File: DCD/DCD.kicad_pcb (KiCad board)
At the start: 4 copper layers, 110 x 110 mm, 141 parts, among them J1 UMPS-04-03.5-G-VT-SM-WT, J2 UMPS-04-03.5-G-VT-SM-WT, J3 UMPS-04-03.5-G-VT-SM-WT, J4 UMPS-04-03.5-G-VT-SM-WT, U1 TLV76780DBVR, U10 OPA277UA, U11 DAC8811ICDGKT, U12 DAC8811ICDGKT, U13 OPA277UA, U14 OPA277UA, U2 ADP7182AUJZ-1.8-R7, U3 LP2985-50DBVR, U4 LP2985-18DBVR, U5 LP2985-33DBVR, U6 ADR4550BRZ, U7 ADA4945-1ACPZ-R2, U8 ADA4945-1ACPZ-R2, U9 AD4630-24BBCZ

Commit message: Progress on the layout
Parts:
- removed C20, C21, C22, C23, C26: 100p, Capacitor_SMD:C_0603_1608Metric
- removed C24: 1µF, Capacitor_SMD:C_0603_1608Metric
- removed C25, C34, C35: 1nF, Capacitor_SMD:C_0603_1608Metric
- removed FB17: 470Ω, Inductor_SMD:L_0603_1608Metric
- removed R1, R2, R3, R4, R5, R6, R7, R8, R9: 1k, Resistor_SMD:R_0603_1608Metric
- removed R12, R13: 100, Resistor_SMD:R_0603_1608Metric
- removed TP3: TestPoint, TestPoint:TestPoint_Pad_D1.5mm
- removed U7, U8: ADA4945-1ACPZ-R2, custom_components:LFCSP16_ADA4945-1ACPZ-R2_ADI
- added FB11: 470Ω, Inductor_SMD:L_0603_1608Metric, F.Cu at (159.3, 54.8)
- added FB18: 470Ω, Inductor_SMD:L_0603_1608Metric, F.Cu at (170.2, 59.8)
- added FB19: 470Ω, Inductor_SMD:L_0603_1608Metric, F.Cu at (181.5, 86.2)
- added FB20: 470Ω, Inductor_SMD:L_0603_1608Metric, F.Cu at (149.8, 103.8)
- added J5: Conn_01x02_Pin, Connector_PinHeader_2.54mm:PinHeader_1x02_P2.54mm_Vertical, F.Cu at (159.2, 51.5)
- added N4: M3 Thumbnut, custom_components:ThumbNut-M3, F.Cu at (175.7, 124.1)
- B1: footprint LOBSTER:Screw_DIN933_M3x14mm -> custom_components:Screw_DIN933_M3x14mm
- H15: footprint LOBSTER:ThreadedSpacer_6mm_M3x0.5_5mm -> custom_components:ThreadedSpacer_6mm_M3x0.5_5mm
- N1, N2, N3, N5, N6, N7: footprint LOBSTER:ThumbNut-M3 -> custom_components:ThumbNut-M3
- moved C28 162.3 mm to (178.2, 88.2), turned to 90 degrees
- moved C27 161.0 mm to (176.8, 88.2), turned to 90 degrees
- moved FB12 156.2 mm to (178.2, 111.2)
- moved C29 150.4 mm to (167.8, 87.2), turned to 90 degrees
- moved FB15 138.8 mm to (160.8, 120.8), turned to -135 degrees
- moved C32 138.8 mm to (153.2, 99.8), turned to 45 degrees
- moved U6 138.0 mm to (172.2, 88.8), turned to 180 degrees
- moved C7 135.2 mm to (165.4, 128.5), turned to 180 degrees
- moved C14 134.5 mm to (164.1, 133.5)
- moved C36 134.2 mm to (153.0, 90.5), turned to 45 degrees
- moved FB7 134.1 mm to (151.7, 101.8), turned to 135 degrees
- moved C12 132.7 mm to (160.9, 132.0), turned to 90 degrees
- moved U13 131.6 mm to (172.5, 76.2), turned to 180 degrees
- moved C10 131.5 mm to (162.4, 128.5)
- moved FB3 131.4 mm to (159.4, 135.2), turned to 180 degrees
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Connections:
- C1 pad 2: /ADC/GND -> /ADC/DGND
- C10 pad 1: /ADC/GND -> /ADC/DGND
- C11 pad 1: /ADC/GND -> /ADC/DGND
- C12 pad 2: /ADC/GND -> /ADC/DGND
- C13 pad 2: /ADC/GND -> /ADC/DGND
- C14 pad 2: /ADC/GND -> /ADC/DGND
- C15 pad 2: /ADC/GND -> /ADC/DGND
- C16 pad 2: /ADC/GND -> /ADC/DGND
- C17 pad 1: /ADC/GND -> /ADC/DGND
- C18 pad 2: /ADC/GND -> /ADC/DGND
- C19 pad 2: /ADC/GND -> /ADC/DGND
- C2 pad 2: /ADC/GND -> /ADC/DGND
- C27 pad 2: /ADC/GND -> /ADC/AGND
- C28 pad 2: /ADC/GND -> /ADC/AGND
- C29 pad 2: /ADC/GND -> /ADC/AGND
- C3 pad 2: /ADC/GND -> /ADC/DGND
- C30 pad 2: /ADC/GND -> /ADC/AGND
- C31 pad 2: /ADC/GND -> /ADC/AGND
- C32 pad 2: /ADC/GND -> /ADC/AGND
- C33 pad 2: /ADC/GND -> /ADC/AGND
- C36 pad 1: Net-(U9-IN0-) -> Net-(U9-IN0+)
- C36 pad 2: /ADC/GND -> /ADC/AGND
- C37 pad 1: Net-(U9-IN1-) -> Net-(U9-IN1+)
- C37 pad 2: /ADC/GND -> /ADC/AGND
- C38 pad 2: /ADC/GND -> /ADC/DGND
- C39 pad 2: /ADC/GND -> /ADC/DGND
- C4 pad 2: /ADC/GND -> /ADC/DGND
- C40 pad 2: /ADC/GND -> /ADC/DGND
- C41 pad 2: /ADC/GND -> /ADC/DGND
- C42 pad 2: /ADC/GND -> /ADC/DGND
- C43 pad 2: /ADC/GND -> /ADC/DGND
- C46 pad 2: /ADC/GND -> /ADC/AGND
- C47 pad 2: /ADC/GND -> /ADC/AGND
- C48 pad 2: /ADC/GND -> /ADC/AGND
- C49 pad 2: /ADC/GND -> /ADC/AGND
- C5 pad 2: /ADC/GND -> /ADC/DGND
- C50 pad 2: /ADC/GND -> /ADC/AGND
- C51 pad 1: /PSUs/-1.8V -> /DAC/-1.2V
- C51 pad 2: /ADC/GND -> /ADC/DGND
- C52 pad 2: /ADC/GND -> /ADC/DGND
- C53 pad 2: /ADC/GND -> /ADC/DGND
- C54 pad 2: /ADC/GND -> /ADC/DGND
- C55 pad 2: /ADC/GND -> /ADC/DGND
- C56 pad 2: /ADC/GND -> /ADC/DGND
- C6 pad 2: /ADC/GND -> /ADC/DGND
- C7 pad 2: /ADC/GND -> /ADC/DGND
- C8 pad 2: /ADC/GND -> /ADC/DGND
- C9 pad 2: /ADC/GND -> /ADC/DGND
- FB2 pad 2: /PSUs/-1.8V -> /DAC/-1.2V
- J2 pad 2: Net-(J2-Pin_2) -> /ADC/DGND
- J4 pad 2: /ADC/GND -> /ADC/AGND
- JP1 pad 3: /ADC/GND -> /ADC/AGND
- R14 pad 1: Net-(U7--OUT) -> /ADC/IN0
- R14 pad 2: Net-(U9-IN0-) -> Net-(U9-IN0+)
- R15 pad 1: Net-(U8--OUT) -> /ADC/IN1
- R15 pad 2: Net-(U9-IN1-) -> Net-(U9-IN1+)
- R17 pad 2: /ADC/GND -> /ADC/AGND
- U1 pad 2: /ADC/GND -> /ADC/DGND
- U10 pad 4: /ADC/GND -> /ADC/AGND
- U11 pad 6: /ADC/GND -> /ADC/AGND
- U12 pad 6: /ADC/GND -> /ADC/AGND
- U13 pad 3: /ADC/GND -> /ADC/AGND
- U14 pad 3: /ADC/GND -> /ADC/AGND
- U2 pad 1: /ADC/GND -> /ADC/DGND
- U3 pad 2: /ADC/GND -> /ADC/DGND
- U4 pad 2: /ADC/GND -> /ADC/DGND
- U5 pad 2: /ADC/GND -> /ADC/DGND
- U6 pad 4: /ADC/GND -> /ADC/AGND
- U9 pad A1: /ADC/GND -> /ADC/AGND
- U9 pad A4: /ADC/GND -> /ADC/AGND
- U9 pad A5: /ADC/GND -> /ADC/AGND
- U9 pad B2: /ADC/GND -> /ADC/AGND
- U9 pad B4: /ADC/GND -> /ADC/AGND
- U9 pad B5: /ADC/GND -> /ADC/AGND
- U9 pad B6: /ADC/GND -> /ADC/DGND
- U9 pad B7: /ADC/GND -> /ADC/DGND
- U9 pad C1: Net-(U9-IN0-) -> /ADC/AGND
- U9 pad C2: /ADC/GND -> /ADC/AGND
- U9 pad C3: /ADC/GND -> /ADC/AGND
- U9 pad C4: /ADC/GND -> /ADC/AGND
- U9 pad C5: /ADC/GND -> /ADC/AGND
- U9 pad C6: /ADC/GND -> /ADC/DGND
- U9 pad D1: /ADC/GND -> /ADC/AGND
- U9 pad D4: /ADC/GND -> /ADC/AGND
- U9 pad D5: /ADC/GND -> /ADC/AGND
- U9 pad D6: /ADC/GND -> /ADC/DGND
- U9 pad E1: /ADC/GND -> /ADC/AGND
- U9 pad E4: /ADC/GND -> /ADC/AGND
- U9 pad E5: /ADC/GND -> /ADC/AGND
- U9 pad E6: /ADC/GND -> /ADC/DGND
- U9 pad E7: /ADC/GND -> /ADC/DGND
- U9 pad F2: /ADC/GND -> /ADC/AGND
- U9 pad F3: /ADC/GND -> /ADC/AGND
- U9 pad F4: /ADC/GND -> /ADC/AGND
- U9 pad F5: /ADC/GND -> /ADC/AGND
- U9 pad F6: /ADC/GND -> /ADC/DGND
- U9 pad G1: Net-(U9-IN1-) -> /ADC/AGND
- U9 pad G2: /ADC/GND -> /ADC/AGND
- U9 pad G4: /ADC/GND -> /ADC/AGND
- U9 pad G5: /ADC/GND -> /ADC/AGND
- U9 pad G6: /ADC/GND -> /ADC/DGND
- U9 pad H1: /ADC/GND -> /ADC/AGND
- U9 pad H2: /ADC/GND -> /ADC/AGND
- U9 pad H4: /ADC/GND -> /ADC/AGND
- U9 pad H8: /ADC/GND -> /ADC/DGND
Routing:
- net Net-(U1-OUT): track 0.00 -> 195.6 mm
- net Net-(U3-VOUT): track 0.00 -> 70.2 mm
- net /ADC/7V: track 0.00 -> 59.7 mm
- net /ADC/5V: track 0.00 -> 47.9 mm, vias 0 -> 2
- net /ADC/1.8V: track 0.00 -> 47.2 mm
- net /Comms/DAC_Ext: track 0.00 -> 36.8 mm, vias 0 -> 1
- net /DAC/DAC1: track 0.00 -> 35.2 mm
- net /ADC/SDO0: track 0.00 -> 27.6 mm, vias 0 -> 1
- net /ADC/BSY: track 0.00 -> 26.8 mm, vias 0 -> 1
- net /ADC/~{CS}: track 0.00 -> 25.6 mm, vias 0 -> 1
- net Net-(U6-VOUT): track 0.00 -> 24.2 mm
- net /ADC/SDI: track 0.00 -> 18.4 mm
- net /DAC/3.3V: track 0.00 -> 14.8 mm
- net /ADC/SCK: track 0.00 -> 14.4 mm
- net Net-(J3-Pin_4): track 0.00 -> 13.8 mm, vias 0 -> 1
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
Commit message: Pregrezz
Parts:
- removed the FB11 at (124.0, 102.5)
- moved FB15 6.10 mm to (164.2, 115.8)
- moved C49 2.76 mm to (156.8, 62.0)
- moved FB18 2.24 mm to (171.2, 61.8)
- moved FB20 1.41 mm to (148.8, 102.8)
- moved FB19 0.79 mm to (181.8, 87.0)
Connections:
- J3 pad 1: Net-(J3-Pin_1) -> /Comms/CLK
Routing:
- net /DAC/-1.2V: track 6.26 -> 89.2 mm, vias 0 -> 2
- net /DAC/3.3V: track 14.8 -> 82.1 mm
- net /Comms/VRef: track 0.02 -> 60.6 mm, vias 1 -> 3
- net /ADC/VIO: track 6.01 -> 61.5 mm, vias 0 -> 2
- net Net-(U6-VOUT): track 24.2 -> 74.0 mm, vias 0 -> 2
- net /ADC/7V: track 59.7 -> 79.5 mm, vias 0 -> 4
- net Net-(U1-OUT): track 195.6 -> 199.0 mm
- net /ADC/5V: vias 2 -> 4
- net /ADC/DGND: vias 3 -> 15
- net /ADC/AGND: vias 6 -> 37

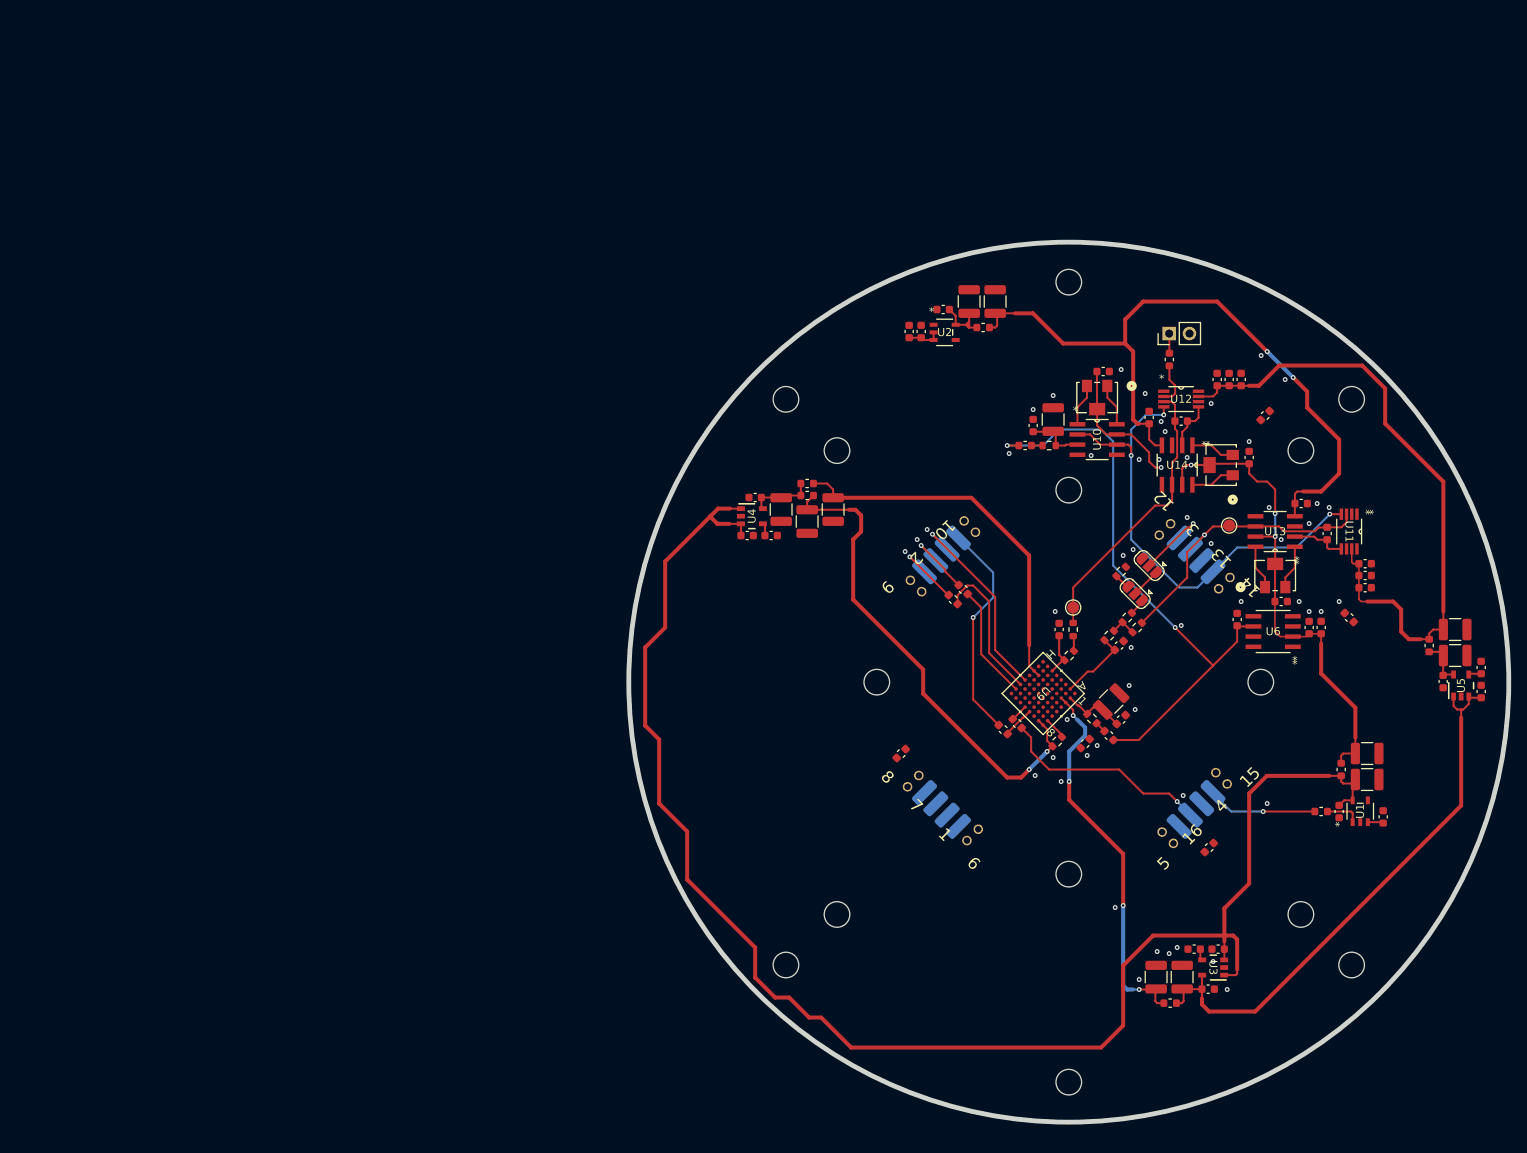
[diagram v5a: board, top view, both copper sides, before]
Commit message: Schematics for the clock reconditioning
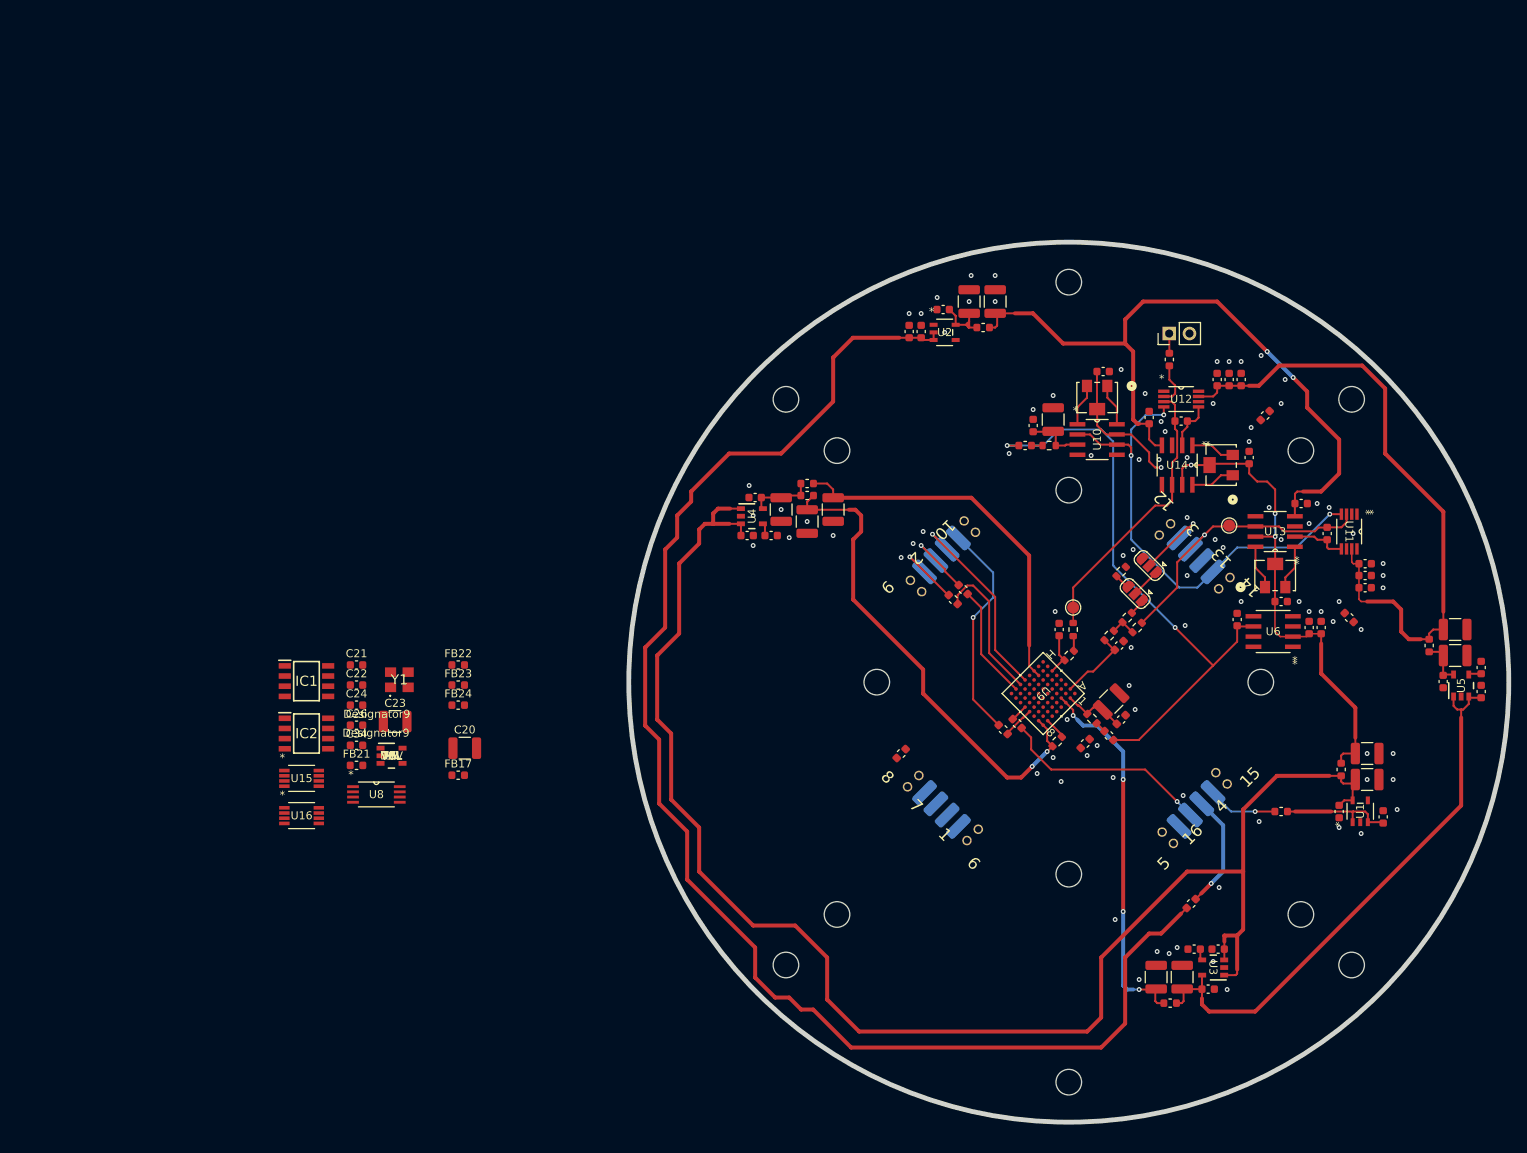
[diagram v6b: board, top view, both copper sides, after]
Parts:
- added C20: 10uF, Capacitor_SMD:C_1210_3225Metric, F.Cu at (71.2, 103.3)
- added C21: 1µF, Capacitor_SMD:C_0603_1608Metric, F.Cu at (57.7, 92.9)
- added C22: 10nF, Capacitor_SMD:C_0603_1608Metric, F.Cu at (57.7, 95.4)
- added C23: 10uF, Capacitor_SMD:C_1210_3225Metric, F.Cu at (62.5, 100.0)
- added C24: 100nF, Capacitor_SMD:C_0603_1608Metric, F.Cu at (57.7, 98.0)
- added C26: 1µF, Capacitor_SMD:C_0603_1608Metric, F.Cu at (57.7, 100.5)
- added C34: 100nF, Capacitor_SMD:C_0603_1608Metric, F.Cu at (57.7, 103.0)
- added FB17: 470Ω, Inductor_SMD:L_0603_1608Metric, F.Cu at (70.4, 106.7)
- added FB21: 470Ω, Inductor_SMD:L_0603_1608Metric, F.Cu at (57.7, 105.5)
- added FB22: 470Ω, Inductor_SMD:L_0603_1608Metric, F.Cu at (70.4, 92.9)
- added FB23: 470Ω, Inductor_SMD:L_0603_1608Metric, F.Cu at (70.4, 95.4)
- added FB24: 470Ω, Inductor_SMD:L_0603_1608Metric, F.Cu at (70.4, 98.0)
- added IC1: 830S21AMI-01LF, custom_components:SOIC127P600X175-8N, F.Cu at (51.4, 95.0)
- added IC2: 830S21AMI-01LF, custom_components:SOIC127P600X175-8N, F.Cu at (51.4, 101.5)
- added U15: MC100EP31DTG, custom_components:TSSOP8_3P10X3P10_ONS, F.Cu at (50.8, 107.1)
- added U16: MC100EP31DTG, custom_components:TSSOP8_3P10X3P10_ONS, F.Cu at (50.8, 111.8)
- added U7: LP2985-33DBVR, custom_components:DBV0005A_N, F.Cu at (62.1, 104.3)
- added U8: CDCLVC1104PWR, custom_components:PW8, F.Cu at (60.2, 109.1)
- added Y1: SiT8208AI-21-33E-50.000000, custom_components:QFN_3225_4pins, F.Cu at (63.0, 94.8)
- moved FB15 7.35 mm to (162.0, 122.8)
- moved FB12 5.00 mm to (173.2, 111.2)
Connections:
- J2 pad 3: /ADC/CNV -> /Comms/Signal Reconditioning/CNV
- J2 pad 4: /Comms/*CS -> /Comms/Signal Reconditioning/*CS
- J3 pad 1: /Comms/CLK -> /Comms/Signal Reconditioning/CLK
- R16 pad 1: /ADC/VIO -> Net-(FB22-Pad1)
- U9 pad A3: /ADC/5V -> Net-(FB24-Pad1)
- U9 pad A8: /ADC/VIO -> Net-(FB22-Pad1)
- U9 pad B3: /ADC/5V -> Net-(FB24-Pad1)
- U9 pad B8: /ADC/VIO -> Net-(FB22-Pad1)
- U9 pad G3: /ADC/1.8V -> Net-(FB23-Pad1)
- U9 pad H3: /ADC/1.8V -> Net-(FB23-Pad1)
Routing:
- net /Comms/-Vin: track 4.12 -> 181.0 mm
- net Net-(J3-Pin_3): track 0.00 -> 14.4 mm, vias 0 -> 1
- net /Comms/+Vin: track 6.33 -> 14.5 mm
- net Net-(J3-Pin_4): track 13.8 -> 8.78 mm
- net Net-(U1-OUT): track 199.0 -> 199.9 mm
- net /ADC/5V: track 47.9 -> 47.3 mm
- net /ADC/DGND: vias 15 -> 50
- net /ADC/AGND: vias 37 -> 39
